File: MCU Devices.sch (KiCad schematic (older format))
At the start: 82 parts, among them J1 END_X, J10 FAN_1, J11 TEMP_BED, J12 TEMP_E0, J13 TEMP_E1, J14 AXIS_X, J15 AXIS_Y, J16 E0, J17 E1, J18 HEAT_BED, J2 END_Y, J22 HEAT_E0, J23 HEAT_E1, J3_1 AXIS_Z1, J3_2 AXIS_Z2, J4 END_Z, J6 END_E0, J7 END_E1, J9 FAN_0, Q1 DMN3713U, Q10 BCX56, Q11 BCX51, Q12 BCX56, Q13 BCX51, Q14 BCX56, Q15 BCX51, Q16 IRLIZ44N, Q17 IRLIZ44N, Q18 IRLIZ44N, Q2 DMN3713U, Q3 BC817, Q4 BC817, Q5 BC817

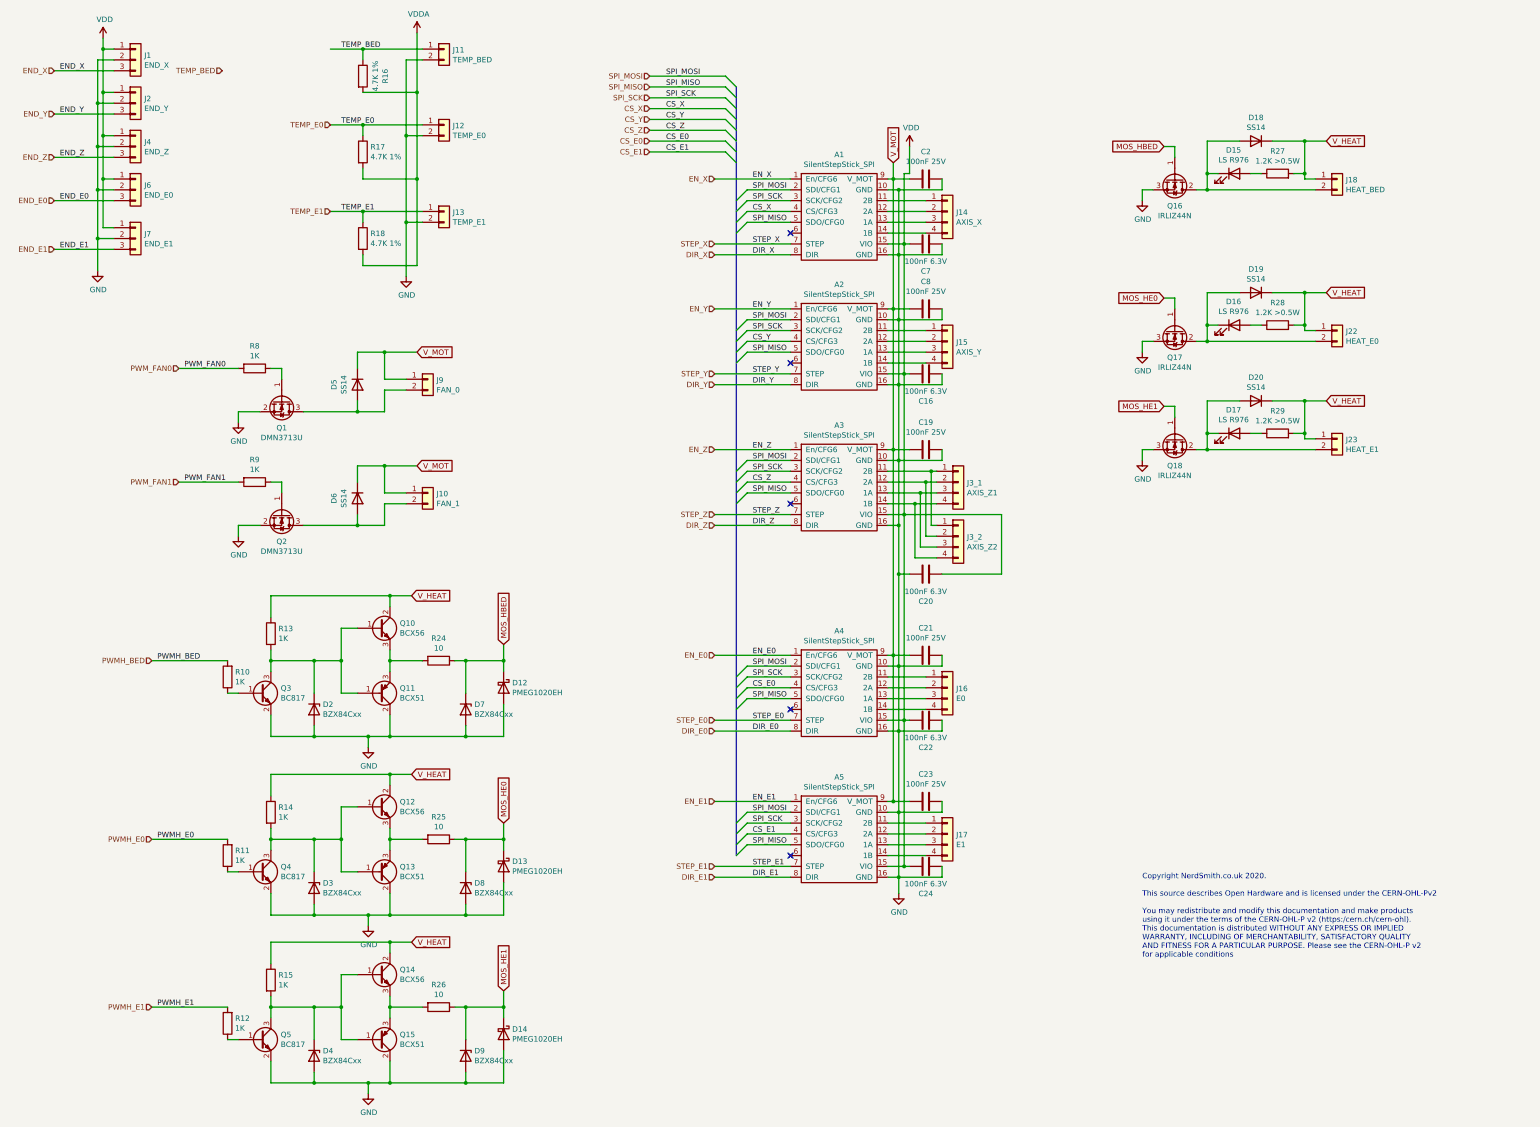
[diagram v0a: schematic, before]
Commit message: Added I2C and 3.3v breakout for expansion port
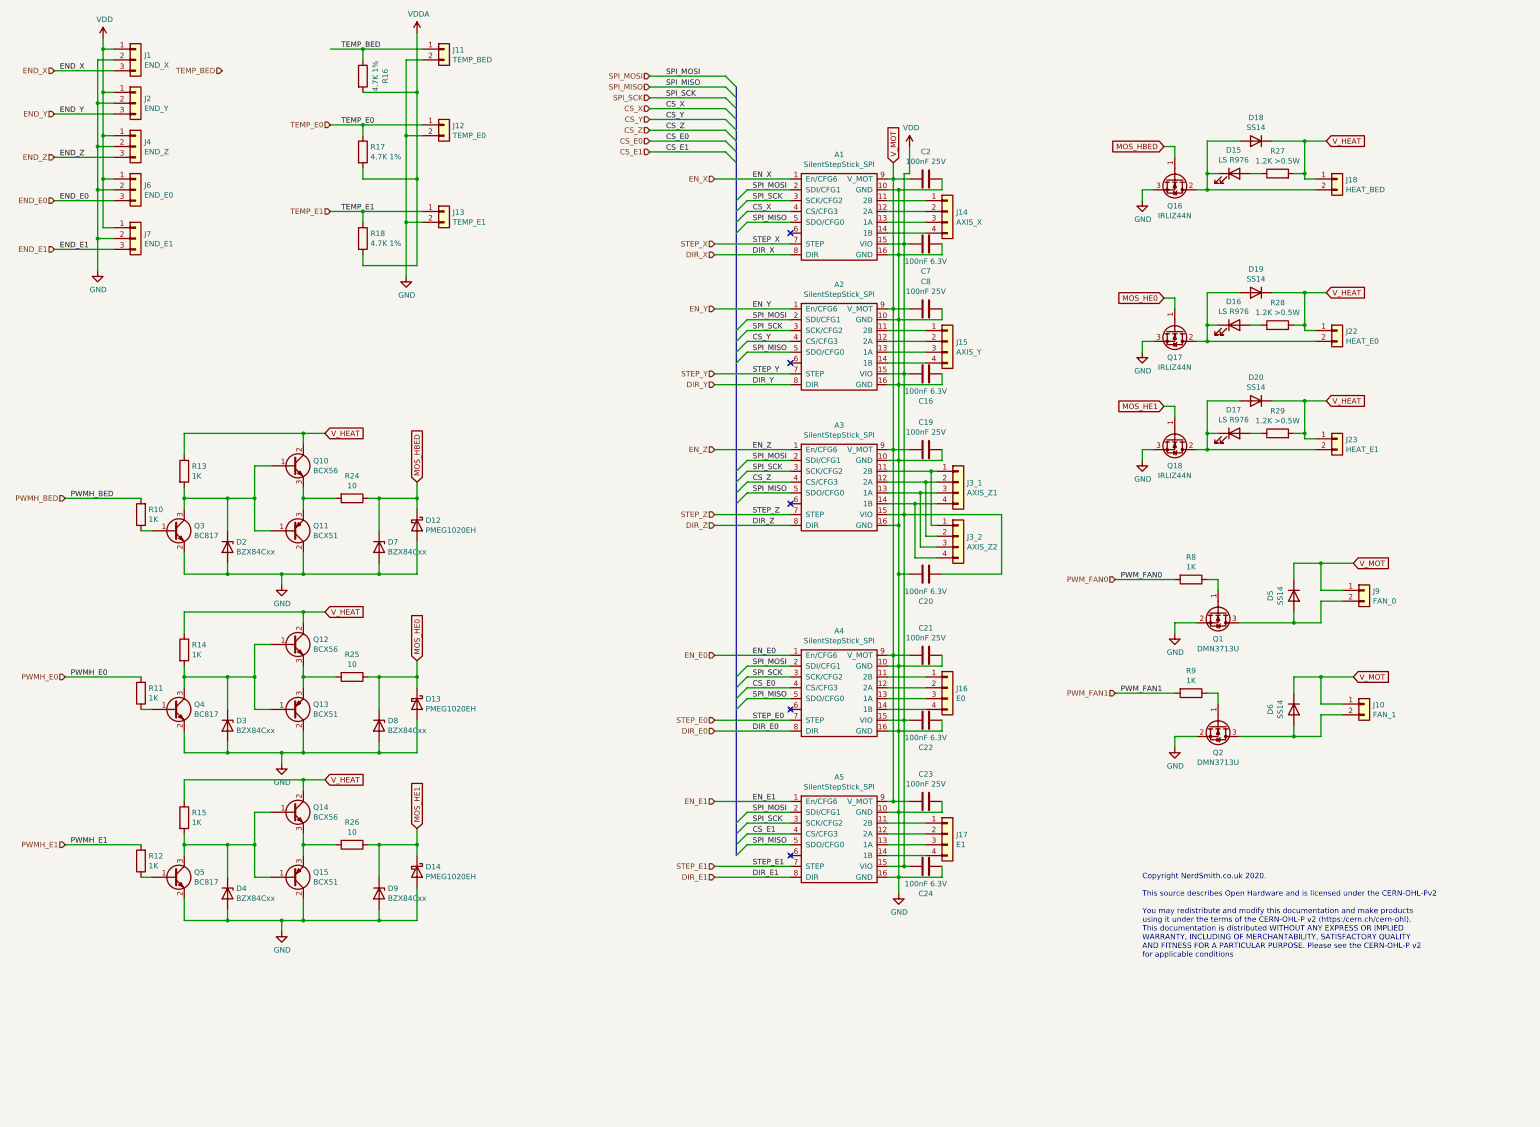
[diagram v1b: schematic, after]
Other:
- moved on the sheet: D12, D13, D14, D2, D3, D4, D5, D6, D7, D8, D9, J10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
